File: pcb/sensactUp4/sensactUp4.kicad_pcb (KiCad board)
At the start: 2 copper layers, 70 x 70 mm, 134 parts, among them J2 IO, J3 BaseConnector, J32 PROG, J5 EXT_ROT, J6 USB, Q1 Q_NMOS_GDS, SW1 Rotary_Encoder_Switch_with_Mo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, SW3 TERM OFF, SW4 RESET, U10 DS18B20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

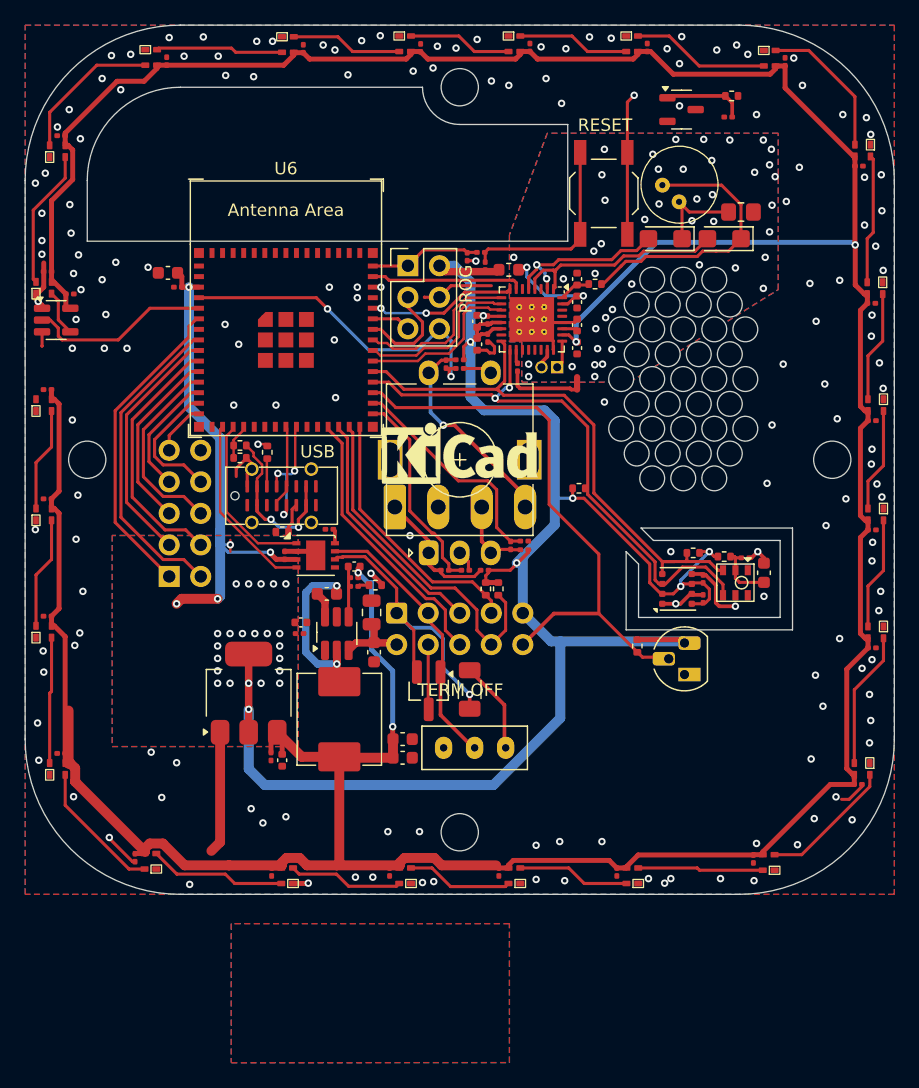
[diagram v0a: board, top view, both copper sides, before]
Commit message: Added 4ch mosfet (DRC nok!)
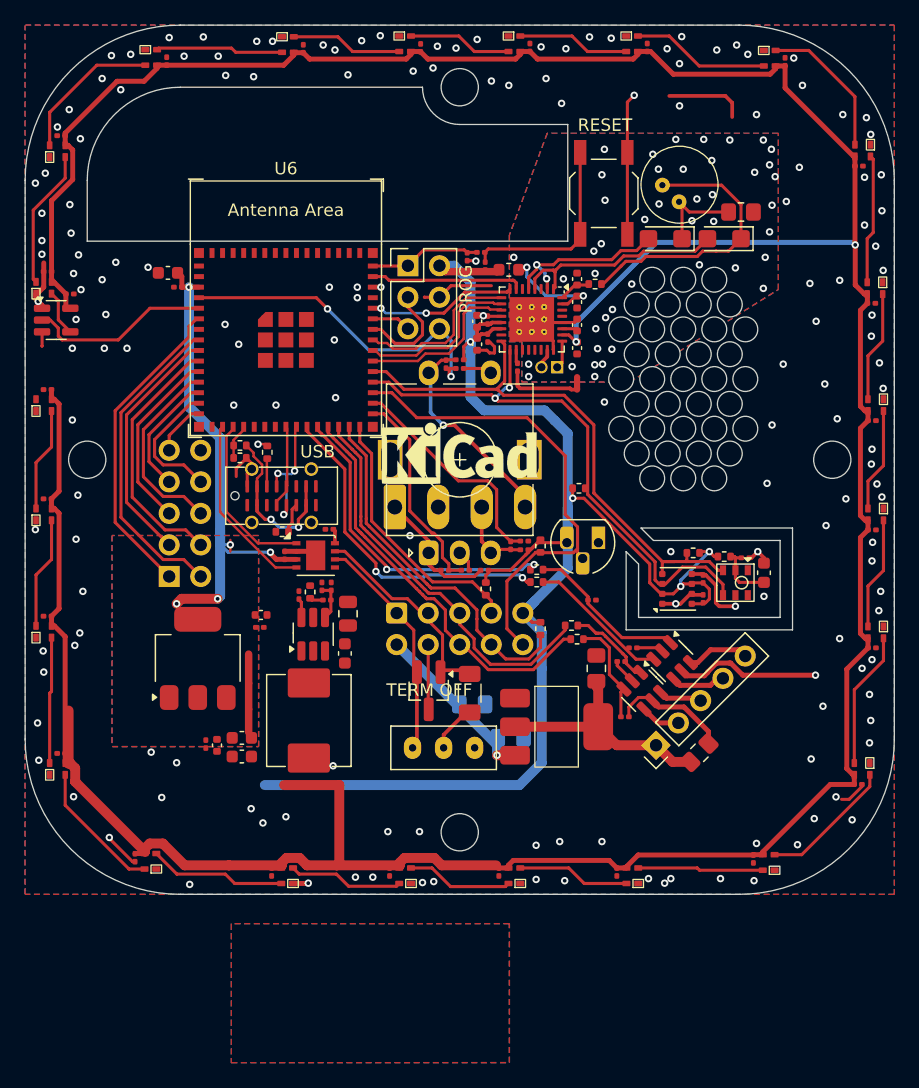
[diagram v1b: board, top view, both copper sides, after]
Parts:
- removed Q1: Q_NMOS_GDS, Package_TO_SOT_SMD:SOT-23-3
- added C48: 10u, Capacitor_SMD:C_0805_2012Metric_Pad1.18x1.45mm_HandSolder, B.Cu at (101.0, 119.7)
- added C53: u1, Capacitor_SMD:C_0805_2012Metric_Pad1.18x1.45mm_HandSolder, B.Cu at (104.1, 122.4)
- added C54: u1, Capacitor_SMD:C_0805_2012Metric_Pad1.18x1.45mm_HandSolder, F.Cu at (111.0, 116.8)
- added C55: 10u, Capacitor_SMD:C_0805_2012Metric_Pad1.18x1.45mm_HandSolder, F.Cu at (119.3, 123.6)
- added J7: Conn_01x05, Connector_PinHeader_2.54mm:PinHeader_1x05_P2.54mm_Vertical, F.Cu at (115.8, 123.0)
- added Q2: AO6800-HXY, Package_TO_SOT_SMD:SOT-23-6, F.Cu at (114.7, 118.6)
- added Q3: AO6800-HXY, Package_TO_SOT_SMD:SOT-23-6, F.Cu at (117.1, 116.2)
- added R56: 1k, Resistor_SMD:R_0402_1005Metric, F.Cu at (109.5, 114.5)
- added R57: 1k, Resistor_SMD:R_0402_1005Metric, F.Cu at (106.2, 108.8)
- added R58: 1k, Resistor_SMD:R_0402_1005Metric, F.Cu at (106.2, 109.8)
- added R62: M1, Resistor_SMD:R_0201_0603Metric, F.Cu at (113.3, 120.7)
- added R63: M1, Resistor_SMD:R_0201_0603Metric, F.Cu at (110.7, 111.3)
- added R64: M1, Resistor_SMD:R_0201_0603Metric, F.Cu at (114.0, 115.2)
- added U7: AMS1117-12, liebler_SEMICONDUCTORS:SOT-223-3_TabPin2_HANDSOLDER, F.Cu at (107.8, 121.5)
- C81: footprint Capacitor_SMD:C_0603_1608Metric -> Capacitor_SMD:C_0201_0603Metric
- C82: footprint Capacitor_SMD:C_0402_1005Metric -> Capacitor_SMD:C_0201_0603Metric
- moved R61 44.7 mm to (113.0, 116.2)
- moved R55 44.6 mm to (109.0, 113.3), turned to 0 degrees
- moved C83 13.0 mm to (82.5, 122.4)
- moved C84 13.0 mm to (82.5, 123.9)
- moved U10 12.7 mm to (111.2, 106.7), turned to 180 degrees
- moved R46 11.2 mm to (106.5, 107.0)
- moved C9 5.39 mm to (80.5, 123.0)
- moved C10 5.34 mm to (79.5, 122.9)
- moved R49 5.28 mm to (88.0, 110.7), turned to -90 degrees
- moved U4 4.96 mm to (78.9, 116.0)
- moved R52 4.67 mm to (106.5, 113.6)
- moved C12 3.26 mm to (84.0, 112.5)
- moved C11 3.24 mm to (83.9, 113.5)
- moved C82 3.05 mm to (88.9, 110.2), turned to 90 degrees
- moved SW3 2.50 mm to (98.7, 123.2)
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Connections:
- R12 pad 1: Net-(SW3-A) -> Net-(SW3-B)
- R12 pad 2: CANL -> CANH
- R55 pad 1: unconnected-(R55-Pad1) -> IO10
- SW3 pad 1: Net-(SW3-A) -> unconnected-(SW3-A-Pad1)
- SW3 pad 2: CANH -> Net-(SW3-B)
- SW3 pad 3: unconnected-(SW3-C-Pad3) -> CANL
- U6 pad 25: unconnected-(U6-GPIO21-Pad25) -> IO13
- U6 pad 26: unconnected-(U6-GPIO26-Pad26) -> IO12
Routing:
- net IO13: track 0.00 -> 26.9 mm, vias 0 -> 2
- net IO12: track 0.00 -> 26.4 mm, vias 0 -> 2
- net +5V: track 320.7 -> 295.5 mm, vias 4 -> 3
- net GND: track 77.8 -> 98.6 mm, vias 168 -> 167
- net +3V3: track 188.4 -> 168.2 mm, vias 33 -> 9
- net +12V: track 0.00 -> 19.0 mm
- net /PSU_SW: track 13.8 -> 0.00 mm, vias 2 -> 0
- net Net-(Q3A-G): track 0.00 -> 13.0 mm
- net IO10: track 19.4 -> 32.2 mm
- net Net-(Q3B-G): track 0.00 -> 11.5 mm
- net IO11: track 22.1 -> 33.1 mm
- net Net-(Q2B-G): track 0.00 -> 8.56 mm
- net +24V: track 5.26 -> 13.7 mm, vias 0 -> 1
- net Onewire: track 46.5 -> 38.9 mm
- net Net-(SW3-A): track 7.31 -> 0.00 mm
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
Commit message: Improved layout DRC ok
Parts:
- moved R63 8.94 mm to (119.0, 114.5)
- moved R57 4.19 mm to (110.2, 110.2)
- moved R58 4.17 mm to (110.2, 111.2)
- moved R52 3.89 mm to (103.8, 116.4), turned to 0 degrees
- moved C54 3.76 mm to (107.8, 114.9)
- moved R55 1.66 mm to (110.2, 112.2)
- moved R56 1.52 mm to (110.2, 113.1)
- moved C12 1.51 mm to (83.2, 111.2)
- moved C11 1.38 mm to (83.0, 112.5)
- moved U4 1.20 mm to (78.9, 117.2)
- moved C10 1.12 mm to (80.5, 122.4)
- moved C9 0.89 mm to (79.7, 122.6)
- moved R46 0.86 mm to (106.7, 107.8)
- moved SW3 0.70 mm to (98.0, 123.2)
- moved U7 0.65 mm to (107.2, 121.5)
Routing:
- net +5V: track 295.5 -> 327.8 mm, vias 3 -> 4
- net +3V3: track 168.2 -> 181.3 mm, vias 9 -> 10
- net GND: track 98.6 -> 108.9 mm, vias 167 -> 166
- net /PSU_SW: track 0.00 -> 9.68 mm, vias 0 -> 2
- net +24V: track 13.7 -> 21.0 mm
- net IO13: track 26.9 -> 31.4 mm
- net SCL_EXT: track 29.2 -> 25.2 mm
- net IO12: track 26.4 -> 30.0 mm
- net +12V: track 19.0 -> 15.9 mm
- net Net-(Q3B-G): track 11.5 -> 8.85 mm
- net IO11: track 33.1 -> 35.4 mm, vias 0 -> 1
- net Net-(Q3A-G): track 13.0 -> 10.9 mm
- net Onewire: track 38.9 -> 37.0 mm
- net IO10: track 32.2 -> 30.7 mm, vias 0 -> 1
- added copper zone on B.Cu, net +12V
- added copper zone on F.Cu, net +12V

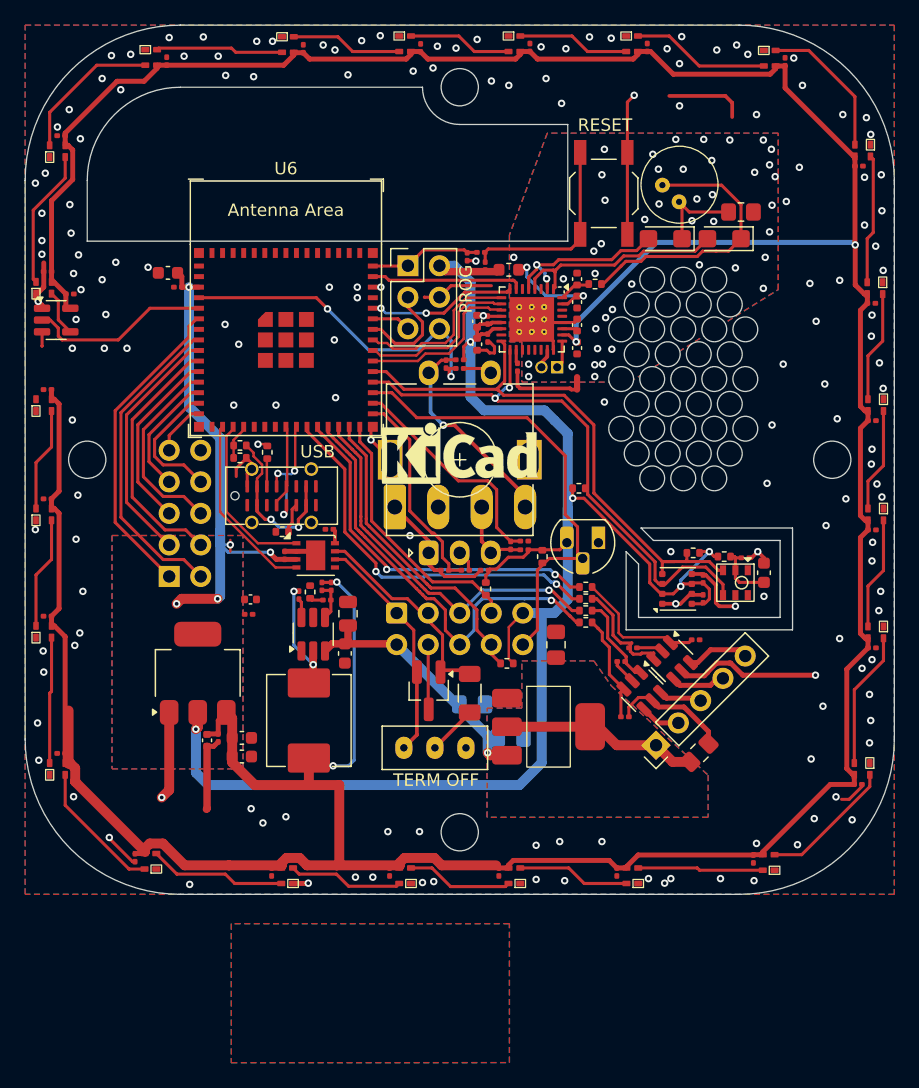
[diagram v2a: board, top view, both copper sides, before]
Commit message: Further layout improvements
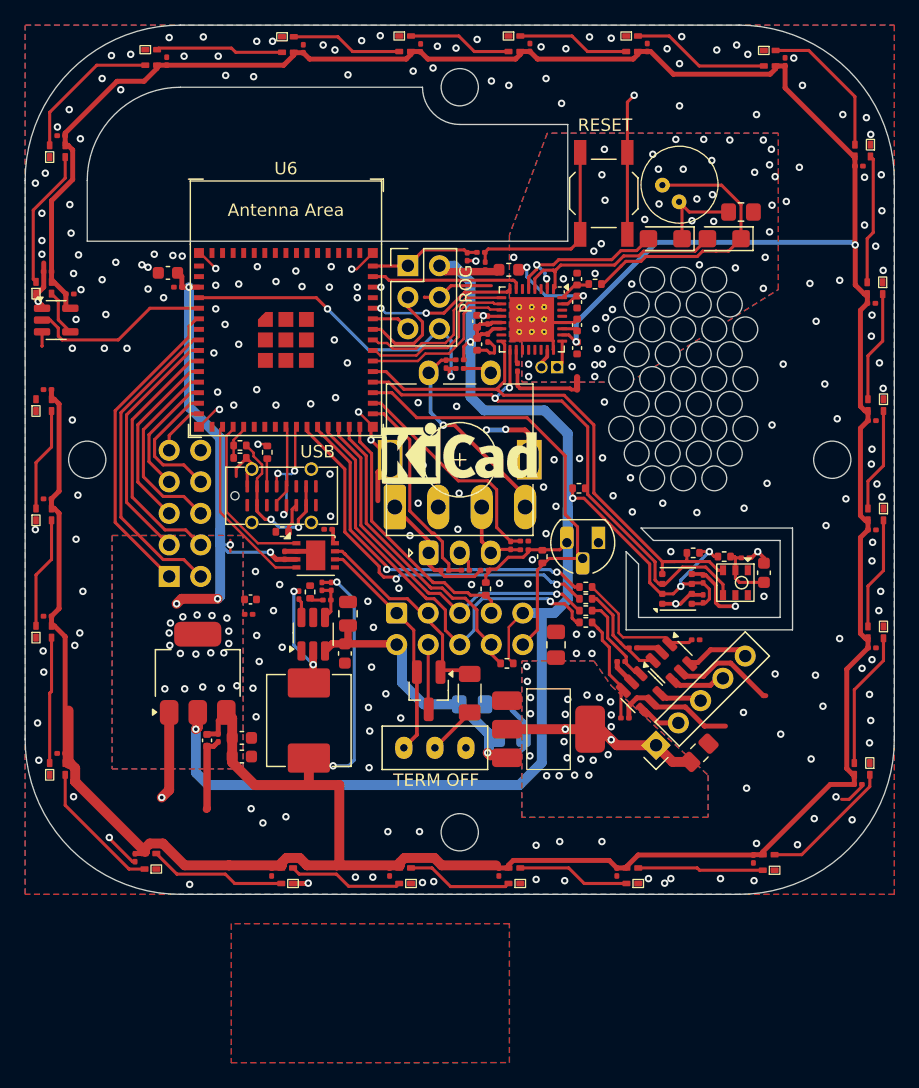
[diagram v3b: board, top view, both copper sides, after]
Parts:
- moved U7 0.20 mm to (107.2, 121.7)
- moved Q2 0.11 mm to (114.7, 118.7)
- moved Q3 0.11 mm to (117.0, 116.3)
- moved R10 0.10 mm to (89.4, 105.6)
- moved R62 0.10 mm to (113.3, 120.8)
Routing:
- net GND: track 108.9 -> 127.9 mm, vias 166 -> 242
- net (no net): track 6.44 -> 0.00 mm, vias 0 -> 1
- net +24V: track 21.0 -> 23.7 mm
- net CANH: track 16.6 -> 15.4 mm
- net +5V: track 327.8 -> 326.9 mm
- net Net-(Q3B-G): track 8.85 -> 8.02 mm
- net +12V: track 15.9 -> 15.3 mm, vias 0 -> 22
- net +3V3: track 181.3 -> 181.2 mm, vias 10 -> 28
